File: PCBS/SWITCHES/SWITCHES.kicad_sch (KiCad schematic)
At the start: 15 parts, among them J1 Conn_01x01_Socket, J2 Conn_01x01_Socket, J3 Conn_01x03_Socket, J6 Conn_01x01_Socket

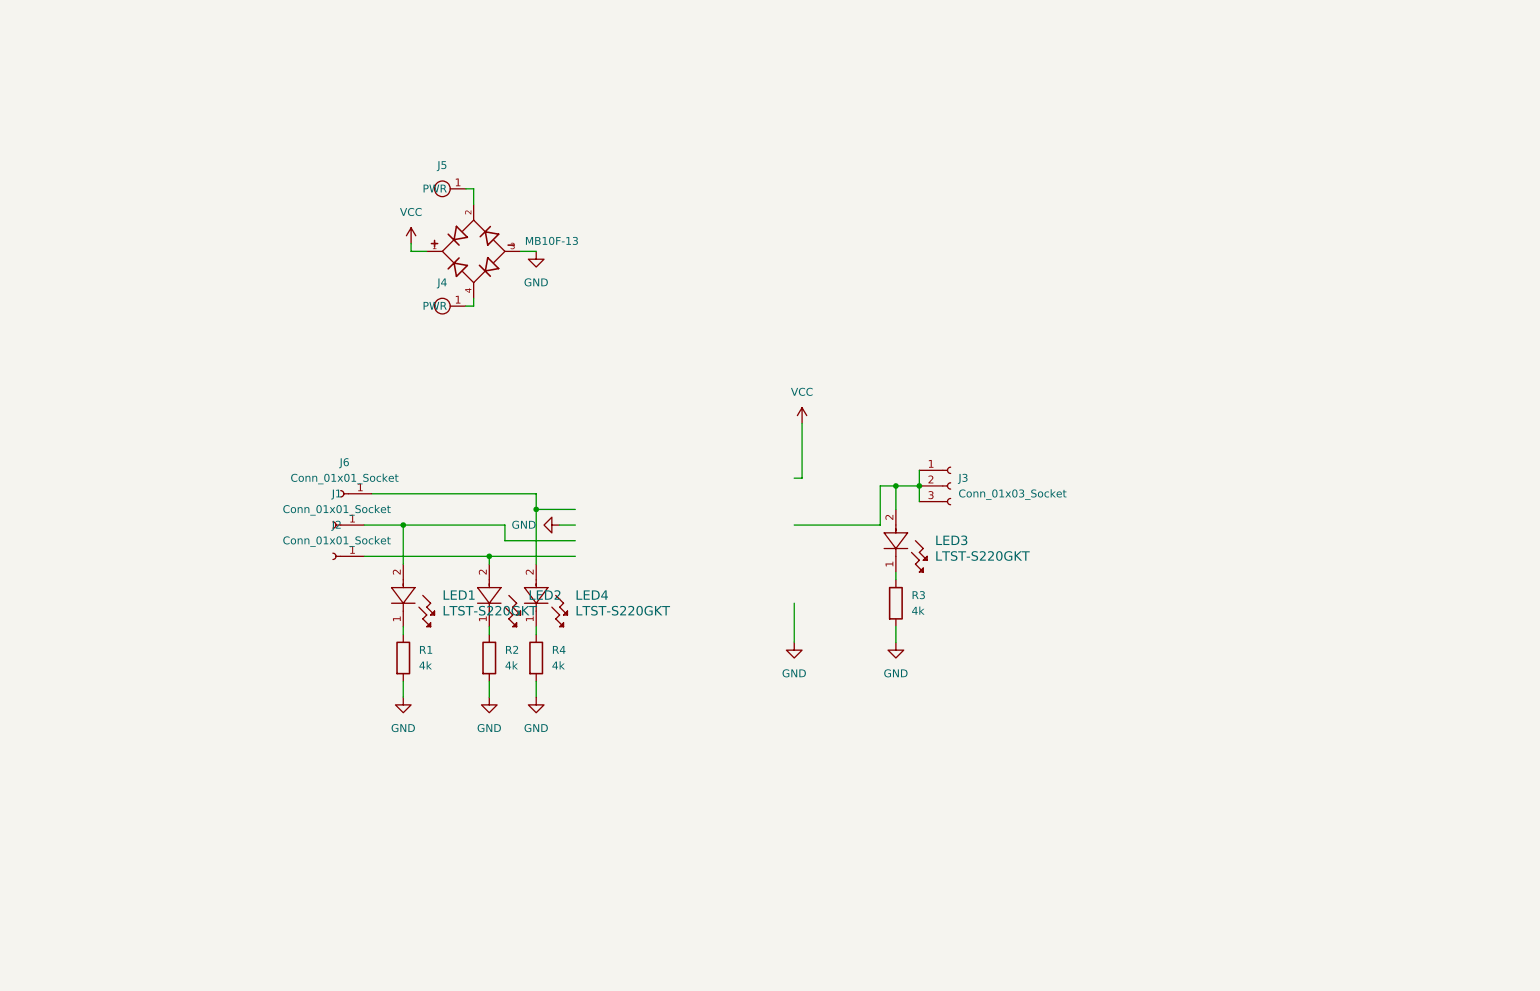
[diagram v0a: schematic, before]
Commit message: Input PCB layout start
4 Rocker Switches will not fit in 1x2 grid size but rotary switch might
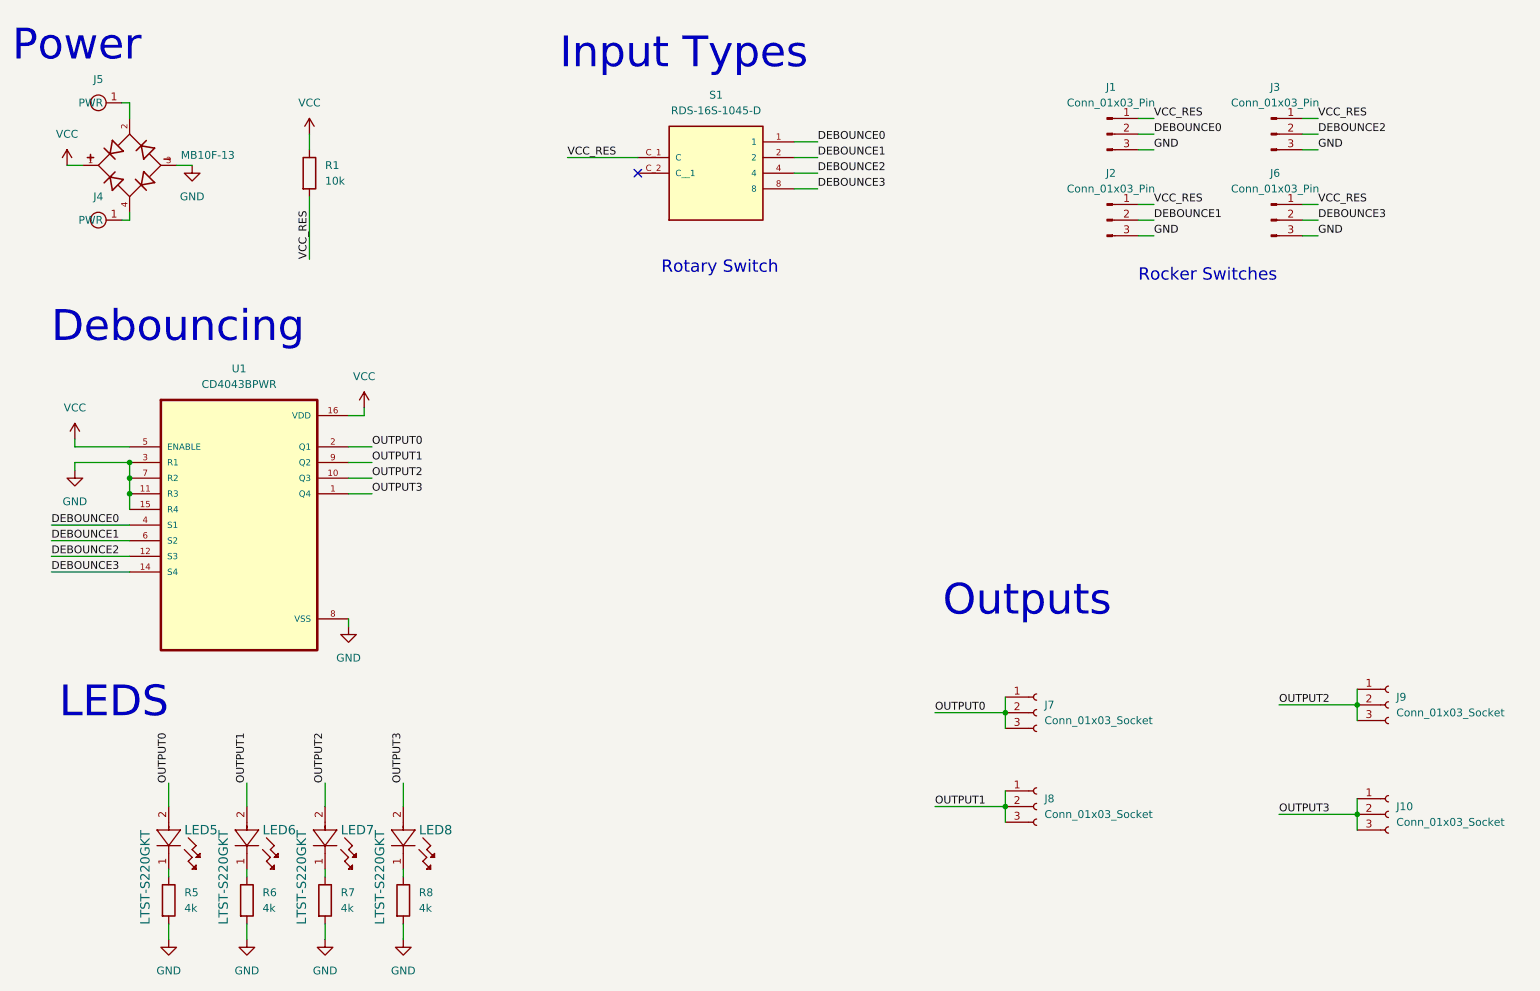
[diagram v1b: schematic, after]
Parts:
- removed J1, J2, J6: Conn_01x01_Socket, Connector_PinSocket_2.54mm:PinSocket_1x01_P2.54mm_Vertical, symbol DigitalLogicLibrary:Conn_01x01_Socket
- removed J3: Conn_01x03_Socket, Connector_PinSocket_2.54mm:PinSocket_1x03_P2.54mm_Vertical, symbol DigitalLogicLibrary:Conn_01x03_Socket
- removed LED1, LED2, LED3, LED4: LTST-S220GKT, LED_LTST-S220GKT_LTO, symbol DigitalLogicLibrary:LTST-S220GKT
- removed R2, R3, R4: 4k, Resistor_SMD:R_0805_2012Metric_Pad1.20x1.40mm_HandSolder, symbol Device:R
- added J1, J2, J3, J6: Conn_01x03_Pin, Connector_PinHeader_2.54mm:PinHeader_1x03_P2.54mm_Horizontal, symbol Connector:Conn_01x03_Pin
- added J10, J7, J8, J9: Conn_01x03_Socket, Connector_PinSocket_2.54mm:PinSocket_1x03_P2.54mm_Vertical, symbol DigitalLogicLibrary:Conn_01x03_Socket
- added LED5, LED6, LED7, LED8: LTST-S220GKT, LED_LTST-S220GKT_LTO, symbol DigitalLogicLibrary:LTST-S220GKT
- added R5, R6, R7, R8: 4k, Resistor_SMD:R_0805_2012Metric_Pad1.20x1.40mm_HandSolder, symbol Device:R
- added S1: RDS-16S-1045-D, DigitalLogicFootprints:SW_RDS-16S-1045-D, symbol DigitalLogicLibrary:RDS-16S-1045-D
- added U1: CD4043BPWR, DigitalLogicFootprints:SOP65P640X120-16N, symbol DigitalLogicLibrary:CD4043BPWR
- R1: value 4k -> 10k
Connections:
- net GND: now also J1.3 (Pin_3), J2.3 (Pin_3), J3.3 (Pin_3), J6.3 (Pin_3), R5.2, R6.2, R7.2, R8.2, U1.11 (R3), U1.15 (R4), U1.3 (R1), U1.7 (R2), U1.8 (VSS); no longer R1.2
- net VCC: now also R1.1, U1.16 (VDD), U1.5 (ENABLE)
- new net: LED6.1, R6.1
- new net: LED8.1, R8.1
- new net: LED5.1, R5.1
- new net: LED7.1, R7.1
- new net DEBOUNCE0: J1.2 (Pin_2), S1.1, U1.4 (S1)
- new net DEBOUNCE1: J2.2 (Pin_2), S1.2, U1.6 (S2)
- new net DEBOUNCE2: J3.2 (Pin_2), S1.4, U1.12 (S3)
- new net DEBOUNCE3: J6.2 (Pin_2), S1.8, U1.14 (S4)
- new net OUTPUT0: J7.1 (Pin_1), J7.2 (Pin_2), J7.3 (Pin_3), LED5.2, U1.2 (Q1)
- new net OUTPUT1: J8.1 (Pin_1), J8.2 (Pin_2), J8.3 (Pin_3), LED6.2, U1.9 (Q2)
- new net OUTPUT2: J9.1 (Pin_1), J9.2 (Pin_2), J9.3 (Pin_3), LED7.2, U1.10 (Q3)
- new net OUTPUT3: J10.1 (Pin_1), J10.2 (Pin_2), J10.3 (Pin_3), LED8.2, U1.1 (Q4)
- new net VCC_RES: J1.1 (Pin_1), J2.1 (Pin_1), J3.1 (Pin_1), J6.1 (Pin_1), R1.2, S1.C_1 (C)
- no-connect marks 0 -> 1
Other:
- note added: "Debouncing"
- note added: "Input Types"
- note added: "LEDS"
- note added: "Outputs"
- note added: "Power"
- note added: "Rocker Switches"
- note added: "Rotary Switch"
- moved on the sheet: J4, J5
